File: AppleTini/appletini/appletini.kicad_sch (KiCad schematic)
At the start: 4 parts, among them J1 Conn_02x25_Counter_Clockwise, Q1 DMG2305UX-7, U16 Pico, U17 Teensy4.1

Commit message: fix some ground issues
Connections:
- net +5V: no longer names the net of J1.25 (Pin_25)
- no-connect marks 59 -> 60
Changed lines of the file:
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@@
   (no_connect (at 236.22 96.52))
   (no_connect (at 161.29 146.05))
+  (no_connect (at 41.91 30.48))
   (no_connect (at 222.25 118.11))
   (no_connect (at 29.21 38.1))
@@
     (stroke (width 0) (type default))
   )
-  (wire (pts (xy 41.91 30.48) (xy 55.88 30.48))
-    (stroke (width 0) (type default))
-  )
   (wire (pts (xy 120.65 130.81) (xy 125.73 130.81))
     (stroke (width 0) (type default))
@@
   )
   (wire (pts (xy 165.1 105.41) (xy 165.1 107.95))
-    (stroke (width 0) (type default))
-  )
-  (wire (pts (xy 55.88 25.4) (xy 55.88 30.48))
     (stroke (width 0) (type default))
   )
@@
         )
       )
-    )
-  )
-  (symbol (lib_id "power:+5V") (at 55.88 25.4 0) (unit 1)
-    (in_bom yes) (on_board yes) (dnp no) (fields_autoplaced)
-    (property "Reference" "#PWR062" (at 55.88 29.21 0)
-      (effects (font (size 1.27 1.27)) hide)
-    )
-    (property "Value" "+5V" (at 55.88 21.59 0)
-      (effects (font (size 1.27 1.27)))
-    )
-    (property "Footprint" "" (at 55.88 25.4 0)
-      (effects (font (size 1.27 1.27)) hide)
-    )
-    (property "Datasheet" "" (at 55.88 25.4 0)
-      (effects (font (size 1.27 1.27)) hide)
-    )
-    (pin "1")
-    (instances
-      (project "appletini"
-        (path "/9f80e081-bf13-4e25-8624-a45101464ae2"
-          (reference "#PWR062") (unit 1)
-        )
-      )

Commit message: Caps on bus power lines
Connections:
- net +5V: now reaches J1.25 (Pin_25)
- net -12V: now reaches J1.33 (Pin_33)
- net -5V: now reaches J1.34 (Pin_34)
- net +12V: now reaches J1.50 (Pin_50)
- no-connect marks 60 -> 56
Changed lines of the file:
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@@
   (no_connect (at 161.29 148.59))
   (no_connect (at 198.12 107.95))
-  (no_connect (at 29.21 50.8))
   (no_connect (at 29.21 55.88))
   (no_connect (at 236.22 96.52))
   (no_connect (at 161.29 146.05))
-  (no_connect (at 41.91 30.48))
   (no_connect (at 222.25 118.11))
   (no_connect (at 29.21 38.1))
@@
   (no_connect (at 229.87 118.11))
   (no_connect (at 29.21 68.58))
-  (no_connect (at 29.21 91.44))
   (no_connect (at 125.73 120.65))
   (no_connect (at 125.73 123.19))
@@
   (no_connect (at 254 97.79))
   (no_connect (at 29.21 58.42))
-  (no_connect (at 29.21 48.26))
   (no_connect (at 254 107.95))
   (no_connect (at 254 102.87))
@@
     (stroke (width 0) (type default))
   )
+  (wire (pts (xy 29.21 91.44) (xy 24.13 91.44))
+    (stroke (width 0) (type default))
+  )
   (wire (pts (xy 254 50.8) (xy 259.08 50.8))
     (stroke (width 0) (type default))
@@
     (stroke (width 0) (type default))
   )
+  (wire (pts (xy 17.78 95.25) (xy 24.13 95.25))
+    (stroke (width 0) (type default))
+  )
   (wire (pts (xy 123.19 125.73) (xy 123.19 138.43))
     (stroke (width 0) (type default))
@@
     (stroke (width 0) (type default))
   )
+  (wire (pts (xy 13.97 50.8) (xy 29.21 50.8))
+    (stroke (width 0) (type default))
+  )
   (wire (pts (xy 41.91 35.56) (xy 60.96 35.56))
     (stroke (width 0) (type default))
@@
     (stroke (width 0) (type default))
   )
+  (wire (pts (xy 24.13 91.44) (xy 24.13 95.25))
+    (stroke (width 0) (type default))
+  )
   (wire (pts (xy 41.91 33.02) (xy 63.5 33.02))
     (stroke (width 0) (type default))
@@
     (stroke (width 0) (type default))
   )
+  (wire (pts (xy 17.78 48.26) (xy 29.21 48.26))
+    (stroke (width 0) (type default))
+  )
   (bus (pts (xy 50.8 81.28) (xy 50.8 83.82))
     (stroke (width 0) (type default))
@@
   )
   (wire (pts (xy 66.04 31.75) (xy 73.66 31.75))
+    (stroke (width 0) (type default))
+  )
+  (wire (pts (xy 41.91 24.13) (xy 41.91 30.48))
     (stroke (width 0) (type default))
   )
@@
         (path "/9f80e081-bf13-4e25-8624-a45101464ae2/2367b025-c7b1-4fa4-8e22-f590856d6590"
           (reference "#PWR029") (unit 1)
+        )
+      )
+    )
+  )
+  (symbol (lib_id "power:-5V") (at 13.97 50.8 0) (unit 1)
+    (in_bom yes) (on_board yes) (dnp no) (fields_autoplaced)
+    (property "Reference" "#PWR023" (at 13.97 48.26 0)
+      (effects (font (size 1.27 1.27)) hide)
+    )
+    (property "Value" "-5V" (at 13.97 46.99 0)
+      (effects (font (size 1.27 1.27)))
+    )
+    (property "Footprint" "" (at 13.97 50.8 0)
+      (effects (font (size 1.27 1.27)) hide)
+    )
+    (property "Datasheet" "" (at 13.97 50.8 0)
+      (effects (font (size 1.27 1.27)) hide)
+    )
+    (pin "1")
+    (instances
+      (project "appletini"
+        (path "/9f80e081-bf13-4e25-8624-a45101464ae2"
+          (reference "#PWR023") (unit 1)
+        )
+      )
+    )
+  )
+  (symbol (lib_id "power:-12V") (at 17.78 48.26 0) (unit 1)
+    (in_bom yes) (on_board yes) (dnp no) (fields_autoplaced)
+    (property "Reference" "#PWR022" (at 17.78 45.72 0)
+      (effects (font (size 1.27 1.27)) hide)
+    )
+    (property "Value" "-12V" (at 17.78 44.45 0)
+      (effects (font (size 1.27 1.27)))
+    )
+    (property "Footprint" "" (at 17.78 48.26 0)
+      (effects (font (size 1.27 1.27)) hide)
+    )
+    (property "Datasheet" "" (at 17.78 48.26 0)
+      (effects (font (size 1.27 1.27)) hide)
+    )
+    (pin "1")
+    (instances
+      (project "appletini"
+        (path "/9f80e081-bf13-4e25-8624-a45101464ae2"
+          (reference "#PWR022") (unit 1)
         )
       )
@@
         )
       )
+    )
+  )
+  (symbol (lib_id "power:+12V") (at 17.78 95.25 0) (unit 1)
+    (in_bom yes) (on_board yes) (dnp no) (fields_autoplaced)
+    (property "Reference" "#PWR024" (at 17.78 99.06 0)
+      (effects (font (size 1.27 1.27)) hide)
+    )
+    (property "Value" "+12V" (at 17.78 91.44 0)
+      (effects (font (size 1.27 1.27)))
+    )
+    (property "Footprint" "" (at 17.78 95.25 0)
+      (effects (font (size 1.27 1.27)) hide)
+    )
+    (property "Datasheet" "" (at 17.78 95.25 0)
+      (effects (font (size 1.27 1.27)) hide)
+    )
+    (pin "1")
+    (instances
+      (project "appletini"
+        (path "/9f80e081-bf13-4e25-8624-a45101464ae2"
+          (reference "#PWR024") (unit 1)
+        )
+      )
+    )
+  )
+  (symbol (lib_id "power:+5V") (at 41.91 24.13 0) (unit 1)
+    (in_bom yes) (on_board yes) (dnp no) (fields_autoplaced)
+    (property "Reference" "#PWR018" (at 41.91 27.94 0)
+      (effects (font (size 1.27 1.27)) hide)
+    )
+    (property "Value" "+5V" (at 41.91 20.32 0)
+      (effects (font (size 1.27 1.27)))
+    )
+    (property "Footprint" "" (at 41.91 24.13 0)
+      (effects (font (size 1.27 1.27)) hide)
+    )
+    (property "Datasheet" "" (at 41.91 24.13 0)
+      (effects (font (size 1.27 1.27)) hide)
+    )
+    (pin "1")
+    (instances
+      (project "appletini"
+        (path "/9f80e081-bf13-4e25-8624-a45101464ae2"
+          (reference "#PWR018") (unit 1)
+        )
+      )

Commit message: part picks and cleanup
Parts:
- Q1: LCSC (none) -> C5261054
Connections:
- net GND: no longer U16.42 (GND)
- no-connect marks 56 -> 34

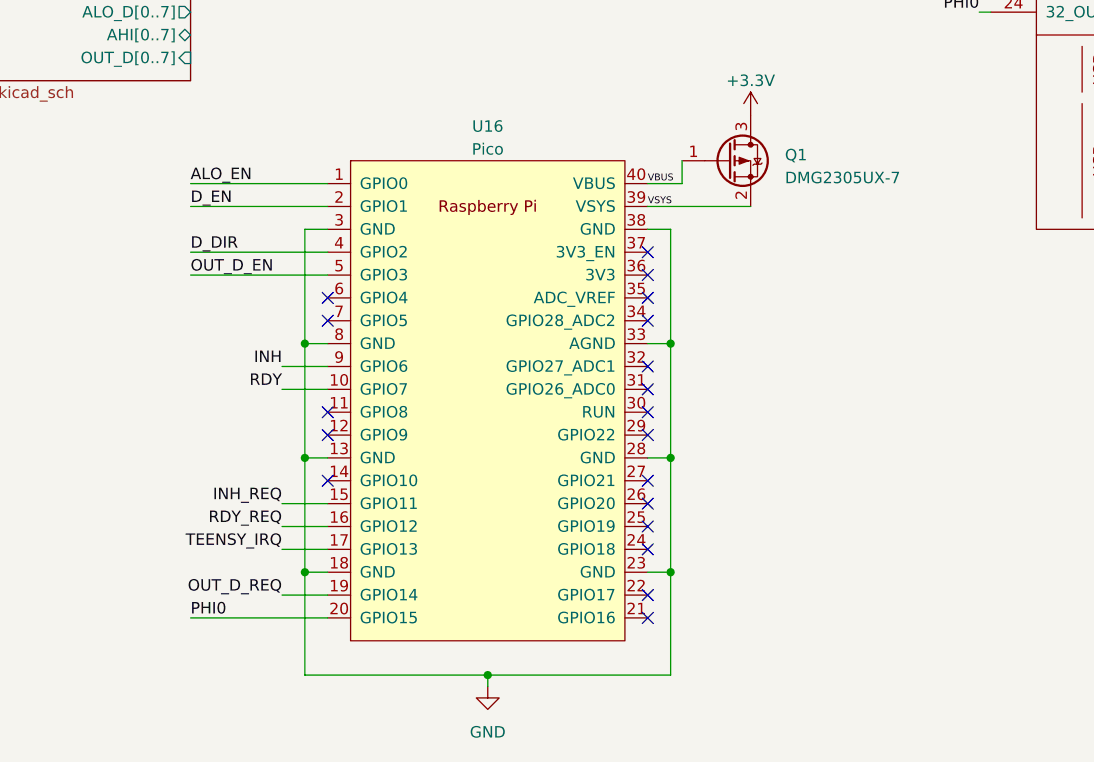
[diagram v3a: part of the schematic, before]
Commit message: Add pico reset, rotate pico to point USB up
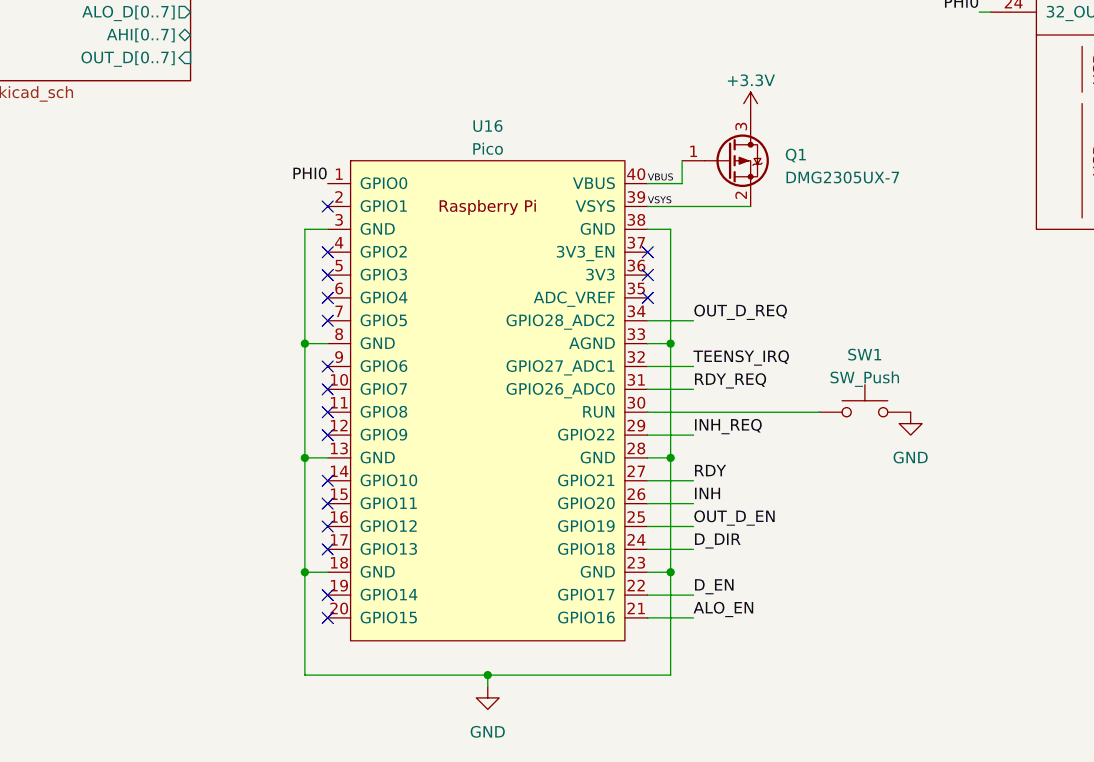
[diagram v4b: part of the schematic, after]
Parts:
- added SW1: SW_Push, Button_Switch_SMD:SW_Push_1P1T_NO_6x6mm_H9.5mm, symbol Switch:SW_Push
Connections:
- net ALO_EN: now also U16.21 (GPIO16); no longer U16.1 (GPIO0)
- net D_DIR: now also U16.24 (GPIO18); no longer U16.4 (GPIO2)
- net D_EN: now also U16.22 (GPIO17); no longer U16.2 (GPIO1)
- net GND: now also SW1.2
- net INH: now also U16.26 (GPIO20); no longer U16.9 (GPIO6)
- net INH_REQ: now also U16.29 (GPIO22); no longer U16.15 (GPIO11)
- net OUT_D_EN: now also U16.25 (GPIO19); no longer U16.5 (GPIO3)
- net OUT_D_REQ: now also U16.34 (GPIO28_ADC2); no longer U16.19 (GPIO14)
- net PHI0: now also U16.1 (GPIO0); no longer U16.20 (GPIO15)
- net RDY: now also U16.27 (GPIO21); no longer U16.10 (GPIO7)
- net RDY_REQ: now also U16.31 (GPIO26_ADC0); no longer U16.16 (GPIO12)
- net TEENSY_IRQ: now also U16.32 (GPIO27_ADC1); no longer U16.17 (GPIO13)
- net at U16.30 (RUN): now also SW1.1
- no-connect marks 34 -> 33

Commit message: 4 layer complete
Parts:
- added JP1: Jumper_2_Open, Connector_PinHeader_2.54mm:PinHeader_1x02_P2.54mm_Vertical, symbol Jumper:Jumper_2_Open
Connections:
- net BUS_DMAOUT is gone; now on net BUS_DMAPASS: J1.24 (Pin_24)
- net +3.3V: no longer Q1.3 (D)
- net +5V: now also Q1.3 (D), JP1.2 (B)
- net VIN: now reaches U17.48 (VIN)
- net VIN: now also JP1.1 (A)
- net BUS_DMAIN renamed BUS_DMAPASS
- no-connect marks 33 -> 32
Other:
- sheet Transceivers ports: added none; removed BUS_DMAIN, BUS_DMAOUT

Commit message: revisions, passed JLCPCB verification
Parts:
- SW1: LCSC (none) -> C410366
- renumbered U16 to U7, U17 to U8
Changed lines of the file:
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@@
   (symbol (lib_id "RPi_Pico:Pico") (at 143.51 132.08 0) (unit 1)
     (in_bom yes) (on_board yes) (dnp no) (fields_autoplaced)
-    (property "Reference" "U16" (at 143.51 101.6 0)
+    (property "Reference" "U7" (at 143.51 101.6 0)
       (effects (font (size 1.27 1.27)))
     )
@@
       (project "appletini"
         (path "/9f80e081-bf13-4e25-8624-a45101464ae2"
-          (reference "U16") (unit 1)
+          (reference "U7") (unit 1)
         )
       )
@@
   (symbol (lib_id "teensy:Teensy4.1") (at 227.33 85.09 0) (unit 1)
     (in_bom yes) (on_board yes) (dnp no) (fields_autoplaced)
-    (property "Reference" "U17" (at 227.33 20.32 0)
+    (property "Reference" "U8" (at 227.33 20.32 0)
       (effects (font (size 1.27 1.27)))
     )
@@
       (project "appletini"
         (path "/9f80e081-bf13-4e25-8624-a45101464ae2"
-          (reference "U17") (unit 1)
+          (reference "U8") (unit 1)
         )
       )
@@
       (effects (font (size 1.27 1.27)) hide)
     )
+    (property "LCSC" "C410366" (at 185.42 133.35 0)
+      (effects (font (size 1.27 1.27)) hide)
+    )

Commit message: change Pico power from 5v to VIN
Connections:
- net +5V: no longer Q1.3 (D)
- net VIN: now also Q1.3 (D)
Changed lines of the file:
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@@
     (effects (font (size 0.762 0.762)) (justify left bottom))
+  )
+  (label "VIN" (at 172.72 100.33 0) (fields_autoplaced)
+    (effects (font (size 1.27 1.27)) (justify left bottom))
   )
   (label "RES" (at 198.12 43.18 180) (fields_autoplaced)
@@
         )
       )
-    )
-  )
-  (symbol (lib_id "power:+5V") (at 172.72 100.33 0) (unit 1)
-    (in_bom yes) (on_board yes) (dnp no) (fields_autoplaced)
-    (property "Reference" "#PWR028" (at 172.72 104.14 0)
-      (effects (font (size 1.27 1.27)) hide)
-    )
-    (property "Value" "+5V" (at 172.72 96.52 0)
-      (effects (font (size 1.27 1.27)))
-    )
-    (property "Footprint" "" (at 172.72 100.33 0)
-      (effects (font (size 1.27 1.27)) hide)
-    )
-    (property "Datasheet" "" (at 172.72 100.33 0)
-      (effects (font (size 1.27 1.27)) hide)
-    )
-    (pin "1")
-    (instances
-      (project "appletini"
-        (path "/9f80e081-bf13-4e25-8624-a45101464ae2"
-          (reference "#PWR028") (unit 1)
-        )
-      )
